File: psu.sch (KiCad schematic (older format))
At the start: 107 parts, among them J1 METER, J3 T1A, J4 T1B, J5 T1C, J6 SENSE+, J7 SENSE-, J8 OUT+, J9 OUT-, Q1 MMBT2907A, Q10 TIP105, Q11 MMBT2907A, Q12 MMBT2907A, Q13 PMP5201Y, Q14 MMBT3904, Q15 MMBT3904, Q16 MMBT3904, Q17 MMBT2907A, Q18 PZT2222A, Q2 MMBT2907A, Q3 MMBT3904, Q4 PMP4201Y, Q5 PMP5201Y, Q6 PMP4201Y, Q7 MMBT3904, Q8 MMBT2907A, Q9 MMBT2907A

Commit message: Changed local regulator circuit, added github readme
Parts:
- removed C4: 47u 10V, symbol C-ALUM-660
- removed Q1, Q2: MMBT2907A, symbol MMBT2907A
- removed R12: 2k2, symbol R-0805
- added Q1, Q2: MMBT3906, symbol MMBT3906
- C3: Manufacturer CDE -> (none); MouserPN 598-AVE106M35C12T-F -> (none); PartNo AVE106M35C12T-F -> (none)
- R11: value 22k -> 560
- R4, R5: value 10k -> 2k2
- R40: value 10k -> 100k
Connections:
- wire segments 279 -> 396
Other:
- note added: "ECO: Renumber\nECO: Check potentiometer rotation directions (library change?)"
- note added: "VOLTAGE REFERENCE and LOCAL REGULATOR"
- note removed: "ECO: Renumber\nECO: Add diodes to D2 for center-tapped (bodge is awkward)\nECO: Widen wire holes\nECO: Check potentiometer rotation directions (library change?)\nECO: Change C9 to same as C4\nECO: D3/DZ2 heat-sharing pad\nECO: Manual note about resistor source not mattering"
- note removed: "ERROR AMP\nBIAS"
- note removed: "LOCAL\nREGULATOR"
- note removed: "VOLTAGE REFERENCE"
- moved on the sheet: C5, D1, D2, D3, D4, D5, D6, D7, J3, J4, J5, Q4A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

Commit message: Rev C in progress
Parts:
- removed C1: 1000u 63V, symbol C-ALUM-16MM
- removed C10: 47u 63V, symbol C-ALUM-6.3MM
- removed C2: 47u, symbol C-ALUM-8MM
- removed C3: 10u, symbol C-ALUM-530
- removed C6: 33p 50V, symbol C-0805
- removed C7: 47u 10V, symbol C-ALUM-660
- removed C8: 10n, symbol C-0805
- removed D1: GBU 100V, symbol BRIDGE
- removed D10, D11, D12, D13: MMBD4148, symbol MMBD4148
- removed D2, D3: 1N4004, symbol 1N4004
- removed D4, D5, D6, D7: S1A, symbol S1A
- removed J6: SENSE+, symbol HEAD-F1
- removed J7: SENSE-, symbol HEAD-F1
- removed MP1, MP2, MP3, MP4: SCREW, symbol SCREW
- removed Q11, Q12: MMBT2907A, symbol MMBT2907A
- removed Q13, Q5: PMP5201Y, symbol PMP5201Y
- removed Q15: MMBT3904, symbol MMBT3904
- removed R15: 10k 1/2W, symbol R-1210
- removed R17: 150, symbol R-0805
- removed R18: 1k5, symbol R-0805
- removed R40: 100k, symbol R-0805
- removed RV1, RV4: 10k, symbol POT
- removed RV5, RV6: *, symbol POT
- added C1: 1000u 63V, symbol C-ALUM-16mm
- added C10: 1nF 1kV, symbol C-1206
- added C2, C6, C8: 47u 63V, symbol C-ALUM-6.3mm
- added C3: 100p, symbol C-0805
- added C5: 4u7, symbol C-1206
- added D1, D2, D3, D4, D5, D6, D7, D8: S1D, symbol S1D
- added J6: SENSE, symbol HEAD-F2
- added Q1, Q4: MMBT3906, symbol MMBT3906
- added Q10, Q19, Q20: MMBT2907A, symbol MMBT2907A
- added Q15: PZT2222A, symbol PZT2222A
- added Q16: MMBT3904, symbol MMBT3904
- added Q18, Q7: PMP4201Y, symbol PMP4201Y
- added R1, R27: 22k, symbol R-0805
- added R26: 100k, symbol R-0805
- added R28, R29: 1k, symbol R-0805
- added R30: 33, symbol R-0805
- added R31, R32: 10k, symbol R-0805
- added R45: 1Meg, symbol R-1206
- added RV2, RV4: 10k, symbol POT-TRIM
- added RV5, RV6: *, symbol POT-TRIM
- added TP1, TP2, TP3, TP4: GND, symbol TEST
- C4: renamed from C11; value 3n3 -> 1n; BomValueLine (none) -> CAP Ceramic 1nF 16V [0805]; OldReference (none) -> C4
- C7: renamed from C5; BomValueLine (none) -> CAP Ceramic 4.7uF 16V [1206]; OldReference (none) -> C7
- C9: BomValueLine (none) -> CAP Ceramic 4.7uF 16V [1206]; OldReference (none) -> C9
- D10: renamed from D9; OldReference (none) -> D10
- D11: renamed from D14; value S1A -> S1D; BomValueLine (none) -> DIODE 1A 50V [SMA]; OldReference (none) -> D11
- D12: renamed from D15; value S1A -> S1D; BomValueLine (none) -> DIODE 1A 50V [SMA]; OldReference (none) -> D12
- D9: renamed from D8; BomValueLine (none) -> DIODE Signal [SOT-23]; OldReference (none) -> D9
- DS1: value HOT -> LIM; BomValueLine (none) -> INDICATOR LED Red [Panel 6.35mm]; Manufacturer (none) -> Bivar; OldReference (none) -> DS1; PartNo (none) -> PM5RD
- DS2: value LIMIT -> HOT; BomValueLine (none) -> INDICATOR LED Red [Panel 6.35mm]; Manufacturer (none) -> Bivar; OldReference (none) -> DS2; PartNo (none) -> PM5RD
- DZ1: BomValueLine (none) -> DIODE Zener 6.2V 2% [SOT-23]; OldReference (none) -> DZ1
- DZ2: renamed from DZ3; BomValueLine (none) -> DIODE TVS 30V WPIV 33A IRSM [SMC-J]; OldReference (none) -> DZ2
- J1: OldReference (none) -> J1
- J3: OldReference (none) -> J3; PartNo (none) -> 60824-1
- J4: OldReference (none) -> J4; PartNo (none) -> 60824-1
- J5: OldReference (none) -> J5; PartNo (none) -> 60824-1
- J8: OldReference (none) -> J8; PartNo (none) -> 60824-1
- J9: OldReference (none) -> J9; PartNo (none) -> 60824-1
- Q11: renamed from Q6; BomValueLine (none) -> TRANS NPN Matched [SOT-363]; OldReference (none) -> Q11
- Q12: renamed from Q7; BomValueLine (none) -> TRANS NPN [SOT-23]; OldReference (none) -> Q12
- Q13: renamed from Q8; BomValueLine (none) -> TRANS PNP 60V [SOT-23]; OldReference (none) -> Q13
- Q14: BomValueLine (none) -> TRANS NPN [SOT-23]; OldReference (none) -> Q14
- Q17: renamed from Q10; BomValueLine (none) -> TRANS PNP Darlington hFE>=1000 60V w/Diode [TO-220]; OldReference (none) -> Q17
- Q2: renamed from Q3; BomValueLine (none) -> TRANS NPN [SOT-23]; OldReference (none) -> Q2
- Q21: renamed from Q17; BomValueLine (none) -> TRANS PNP [SOT-23]; OldReference (none) -> Q21
- Q22: renamed from Q16; BomValueLine (none) -> TRANS NPN [SOT-23]; OldReference (none) -> Q22
- Q3: renamed from Q18; BomValueLine (none) -> TRANS NPN [SOT-223]; OldReference (none) -> Q3
- Q5: renamed from Q2; BomValueLine (none) -> TRANS PNP [SOT-23]; OldReference (none) -> Q5
- Q6: renamed from Q1; BomValueLine (none) -> TRANS PNP [SOT-23]; OldReference (none) -> Q6
- Q8: renamed from Q4; BomValueLine (none) -> TRANS NPN Matched [SOT-363]; OldReference (none) -> Q8
- Q9: BomValueLine (none) -> TRANS PNP [SOT-23]; OldReference (none) -> Q9
- R10: renamed from R11; value 560 -> 470; BomValueLine (none) -> RES 470 5% [0805]; OldReference (none) -> R10
- R11: renamed from R6; value 12k -> 100k; BomValueLine (none) -> RES 100k 5% [0805]; OldReference (none) -> R11
- R12: renamed from R8; value 62k 1% -> 22k; BomValueLine (none) -> RES 22k 5% [0805]; OldReference (none) -> R12
- R13: renamed from R7; value 56k 1% -> 22k; BomValueLine (none) -> RES 22k 5% [0805]; OldReference (none) -> R13
- R14: renamed from R9; BomValueLine (none) -> RES 22k 0.5% [0805]; OldReference (none) -> R14
- R15: renamed from R10; BomValueLine (none) -> RES 22k 0.5% [0805]; OldReference (none) -> R15
- R16: BomValueLine (none) -> RES 1k 5% [0805]; OldReference (none) -> R16
- R17: renamed from R14; BomValueLine (none) -> RES 1k 5% [0805]; OldReference (none) -> R17
- R18: renamed from R13; OldReference (none) -> R18
- R19: value 820 -> 1k; BomValueLine (none) -> RES 1k 5% [0805]; OldReference (none) -> R19
- R2: value 4k7 -> 22k; BomValueLine (none) -> RES 22k 5% [0805]; OldReference (none) -> R2
- R20: value 12k -> 1k; BomValueLine (none) -> RES 1k 5% [0805]; OldReference (none) -> R20
- R21: value 1k -> 22k; BomValueLine (none) -> RES 22k 5% [0805]; OldReference (none) -> R21
- R22: BomValueLine (none) -> RES 1k 5% [0805]; OldReference (none) -> R22
- R23: value 10k -> 22k; BomValueLine (none) -> RES 22k 5% [0805]; OldReference (none) -> R23
- R24: value 8k2 -> 33; BomValueLine (none) -> RES 33 5% [0805]; OldReference (none) -> R24
- R25: BomValueLine (none) -> RES 10k 5% [0805]; OldReference (none) -> R25
- R3: renamed from R39; value 10 -> 33; BomValueLine (none) -> RES 33 5% [0805]; OldReference (none) -> R3
- R33: renamed from R34; BomValueLine (none) -> RES {1 / 0.47 / 1} 5% [1210]; OldReference (none) -> R33
- R34: renamed from R41; value 10k -> 22k; BomValueLine (none) -> RES 22k 5% [0805]; OldReference (none) -> R34
- R35: BomValueLine (none) -> RES {180 68 180} 5% [0805]; OldReference (none) -> R35
- R36: BomValueLine (none) -> RES {27k 15k 27k} 5% [0805]; OldReference (none) -> R36
- R37: renamed from R30; BomValueLine (none) -> RES 120k 0.5% [0805]; OldReference (none) -> R37
- R38: renamed from R31; BomValueLine (none) -> RES 120k 0.5% [0805]; OldReference (none) -> R38
- R39: renamed from R32; BomValueLine (none) -> RES 100 5% [0805]; OldReference (none) -> R39
- R4: value 2k2 -> 22k; BomValueLine (none) -> RES 22k 5% [0805]; OldReference (none) -> R4
- R40: renamed from R33; BomValueLine (none) -> RES 100 5% [0805]; OldReference (none) -> R40
- R41: renamed from R27; value 8k2 -> 10k; BomValueLine (none) -> RES 10k 5% [0805]; OldReference (none) -> R41
- R42: renamed from R26; BomValueLine (none) -> RES 100k 5% [0805]; OldReference (none) -> R42
- R43: renamed from R28; BomValueLine (none) -> RES Therm 100k 5% [Radial]; OldReference (none) -> R43
- R44: renamed from R29; BomValueLine (none) -> RES 270 5% [0805]; OldReference (none) -> R44
- R5: renamed from R37; value 27k -> 22k; BomValueLine (none) -> RES 22k 5% [0805]; OldReference (none) -> R5
- R6: renamed from R38; value 100k -> 18k; BomValueLine (none) -> RES 18k 5% [0805]; OldReference (none) -> R6
- R7: renamed from R3; value 22k -> 10k; BomValueLine (none) -> RES 10k 5% [0805]; OldReference (none) -> R7
- R8: renamed from R1; value 22k -> 10k; BomValueLine (none) -> RES 10k 5% [0805]; OldReference (none) -> R8
- R9: renamed from R5; value 2k2 -> 470; BomValueLine (none) -> RES 470 5% [0805]; OldReference (none) -> R9
- RV1: renamed from RV2; OldReference (none) -> RV1
- RV3: value 5k -> 10k; OldReference (none) -> RV3
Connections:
- net labels added: 1mA 240R, = MMBT2907A or similar (60V), = MMBT3904 or similar, = PMP4201Y, DMMT3904W or similar, = PMP5201Y, DMMT3906W or similar, CGND, GND, GUARD, V-UNREG
- net labels removed: 900uA 240R, = MMBT2907A, = MMBT3904, VBIAS, VCC, VEE
- wire segments 396 -> 291
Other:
- note added: "CURRENT LIMITER"
- note added: "ESR > 0r5"
- note added: "FEEDBACK INPUT"
- note added: "LOCAL REGULATOR"
- note added: "METER TRIM"
- note added: "Matching connector: TE Conn 60598-3\nConnectors are expensive and optional; holes will\ntake 16g wire as well."
- note added: "OUTPUT FILTER"
- note added: "POWER INPUT"
- note added: "R33"
- note added: "VOLTAGE REFERENCE"
- note removed: "CURRENT REFERENCE AND BIAS"
- note removed: "CURRENT SENSE RESISTOR"
- note removed: "CURRENT SENSE\nAMPLIFIER/\nCOMPARATOR"
- note removed: "ECO: Renumber\nECO: Check potentiometer rotation directions (library change?)"
- note removed: "MAIN\nRECTIFIER"
- note removed: "OUTPUT FILTER\nAND PROTECTION"
- note removed: "R34"
- note removed: "VOLTAGE REFERENCE and LOCAL REGULATOR"
- moved on the sheet: C4, C7, C9, D10, D11, D12, D9, DZ1, DZ2, J1, J3, J4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

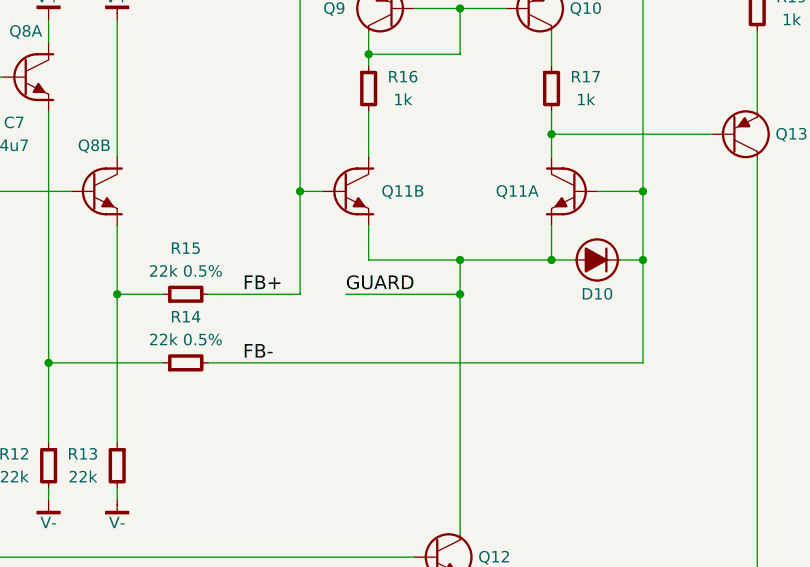
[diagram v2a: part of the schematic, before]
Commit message: Added beginning of simulation
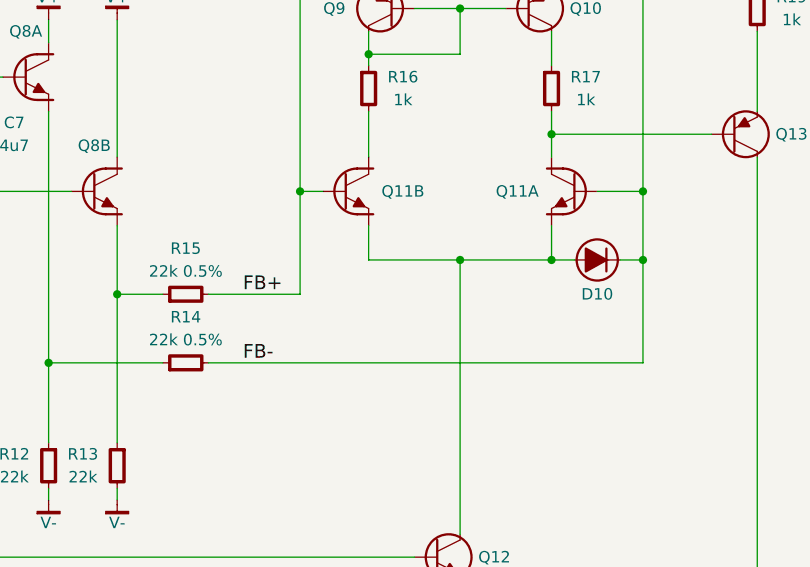
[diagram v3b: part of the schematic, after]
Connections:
- net labels removed: GUARD
- wire segments 291 -> 290
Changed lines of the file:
@@
 Connection ~ 5500 10000
-Wire Wire Line
-	7500 5150 7000 5150
-Connection ~ 7500 5150
-Text Label 7000 5150 0    60   ~ 0
-GUARD
 Wire Wire Line
 	10450 4600 10450 4700

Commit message: Few BOM-related changes
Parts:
- added DS3: POWER, symbol LED
- D10: BomValueLine (none) -> DIODE Signal [SOT-23]
- Q4: BomValueLine TRANS PNP 60V [SOT-23] -> TRANS PNP [SOT-23]
- R2: value 22k -> 10k; BomValueLine RES 22k 5% [0805] -> (none); OldReference R2 -> (none)
- R37, R38: value 120k 0.5% -> * 0.5%
- R39, R40: value 100 -> 270
- R45: BomValueLine (none) -> RES 1M 5% [1206]
- RV3: value 10k -> 1k
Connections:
- net labels added: 1A 125V SB
- net labels removed: 750mA 125V SB
- wire segments 290 -> 292
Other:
- note added: "120k"
- note added: "75k"
- note added: "Coupled\nto Q17"
- note added: "R37"
- note added: "R37, R38: 120k 75k 75k"
- note added: "R38"
- note removed: "Coupled\nto Q9"
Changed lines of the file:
@@
 F 2 "" H 8100 5000 60  0000 C CNN
 F 3 "" H 8100 5000 60  0000 C CNN
-F 4 "D10" H 8100 5000 50  0001 C CNN "OldReference"
+F 4 "DIODE Signal [SOT-23]" H 8100 5000 60  0001 C CNN "BomValueLine"
+F 5 "D10" H 8100 5000 50  0001 C CNN "OldReference"
 	1    8100 5000
 	0    -1   -1   0
@@
 P 12500 2200
 F 0 "R37" V 12300 2200 50  0000 C CNN
-F 1 "120k 0.5%" V 12400 2200 50  0000 C CNN
+F 1 "* 0.5%" V 12400 2200 50  0000 C CNN
 F 2 "" H 12500 2250 60  0000 C CNN
 F 3 "" H 12500 2250 60  0000 C CNN
@@
 P 13000 2300
 F 0 "R38" V 12700 2300 50  0000 C CNN
-F 1 "120k 0.5%" V 12800 2300 50  0000 C CNN
+F 1 "* 0.5%" V 12800 2300 50  0000 C CNN
 F 2 "" H 13000 2350 60  0000 C CNN
 F 3 "" H 13000 2350 60  0000 C CNN
@@
 P 13200 2800
 F 0 "R39" H 13350 2750 50  0000 C CNN
-F 1 "100" H 13350 2850 50  0000 C CNN
+F 1 "270" H 13350 2850 50  0000 C CNN
 F 2 "" H 13200 2850 60  0000 C CNN
 F 3 "" H 13200 2850 60  0000 C CNN
@@
 P 15000 7450
 F 0 "#FFP1" V 14900 7450 50  0001 C CNN
-F 1 "750mA 125V SB" V 14800 7450 50  0000 C CNN
+F 1 "1A 125V SB" V 14800 7450 50  0000 C CNN
 F 2 "" H 15000 7500 60  0000 C CNN
 F 3 "" H 15000 7500 60  0000 C CNN
@@
 $EndComp
 Text Notes 5650 2500 2    50   ~ 0
-Coupled\nto Q9
+Coupled\nto Q17
 $Comp
 L VA_METER #MFP1
@@
 P 15900 5150
 F 0 "#MFP1" H 16150 5100 50  0001 C CNN
-F 1 "1mA 240R" H 16250 5100 50  0000 C CNN
+F 1 "1mA 240R" H 16250 5200 50  0000 C CNN
 F 2 "" H 15900 5300 60  0000 C CNN
 F 3 "" H 15900 5300 60  0000 C CNN
 F 4 "METER 1mA full scale w/ custom scale card" H 15900 5150 60  0001 C CNN "BomValueLine"
-F 5 "M(FP)" H 16250 5200 50  0000 C CNN "Option"
+F 5 "M(FP)" H 16250 5100 50  0000 C CNN "Option"
 F 6 "#MFP1" H 15900 5150 50  0001 C CNN "OldReference"
 	1    15900 5150
@@
 	-1   0    0    -1
 $EndComp
-Text Notes 13850 3925 0    50   Italic 10
+Text Notes 13850 3675 0    50   Italic 10
 COMPONENT VALUES
-Text Notes 13850 4050 0    50   ~ 10
+Text Notes 13850 3800 0    50   ~ 10
 *
-Text Notes 14050 4050 0    50   ~ 10
+Text Notes 14050 3800 0    50   ~ 10
 PS-1H
-Text Notes 14400 4050 0    50   ~ 10
+Text Notes 14400 3800 0    50   ~ 10
 PS-1L
-Text Notes 14750 4050 0    50   ~ 10
+Text Notes 14750 3800 0    50   ~ 10
 PS-1LL
-Text Notes 13850 4250 0    50   ~ 10
+Text Notes 13850 4000 0    50   ~ 10
 R35
-Text Notes 14050 4250 0    50   ~ 0
+Text Notes 14050 4000 0    50   ~ 0
 180
-Text Notes 14400 4250 0    50   ~ 0
+Text Notes 14400 4000 0    50   ~ 0
 68
-Text Notes 14750 4250 0    50   ~ 0
+Text Notes 14750 4000 0    50   ~ 0
 180
-Text Notes 13850 4450 0    50   ~ 10
+Text Notes 13850 4200 0    50   ~ 10
 R36
-Text Notes 14050 4450 0    50   ~ 0
+Text Notes 14050 4200 0    50   ~ 0
 27k
-Text Notes 14400 4450 0    50   ~ 0
+Text Notes 14400 4200 0    50   ~ 0
 15k
-Text Notes 14750 4450 0    50   ~ 0
+Text Notes 14750 4200 0    50   ~ 0
 15k
-Text Notes 13850 4350 0    50   ~ 10
+Text Notes 13850 4100 0    50   ~ 10
 RV5
-Text Notes 14050 4350 0    50   ~ 0
+Text Notes 14050 4100 0    50   ~ 0
 500
-Text Notes 14400 4350 0    50   ~ 0
+Text Notes 14400 4100 0    50   ~ 0
 500
-Text Notes 14750 4350 0    50   ~ 0
+Text Notes 14750 4100 0    50   ~ 0
 500
-Text Notes 13850 4550 0    50   ~ 10
+Text Notes 13850 4300 0    50   ~ 10
 RV6
-Text Notes 14050 4550 0    50   ~ 0
+Text Notes 14050 4300 0    50   ~ 0
 20k
-Text Notes 14400 4550 0    50   ~ 0
+Text Notes 14400 4300 0    50   ~ 0
 10k
-Text Notes 14750 4550 0    50   ~ 0
+Text Notes 14750 4300 0    50   ~ 0
 10k
-Text Notes 13850 4150 0    50   ~ 10
+Text Notes 13850 3900 0    50   ~ 10
 R33
-Text Notes 14050 4150 0    50   ~ 0
+Text Notes 14050 3900 0    50   ~ 0
 1R
-Text Notes 14400 4150 0    50   ~ 0
+Text Notes 14400 3900 0    50   ~ 0
 R47
-Text Notes 14750 4150 0    50   ~ 0
+Text Notes 14750 3900 0    50   ~ 0
 1R
 $Comp
@@
 P 14150 2800
 F 0 "R40" H 14000 2750 50  0000 C CNN
-F 1 "100" H 14000 2850 50  0000 C CNN
+F 1 "270" H 14000 2850 50  0000 C CNN
 F 2 "" H 14150 2850 60  0000 C CNN
 F 3 "" H 14150 2850 60  0000 C CNN
@@
 P 10300 4750
 F 0 "RV3" H 10450 4800 50  0000 C CNN
-F 1 "10k" H 10450 4700 50  0000 C CNN
+F 1 "1k" H 10450 4700 50  0000 C CNN
 F 2 "" H 10300 4800 60  0000 C CNN
 F 3 "" H 10300 4800 60  0000 C CNN
@@
 F 2 "" H 5300 9650 60  0000 C CNN
 F 3 "" H 5300 9650 60  0000 C CNN
-F 4 "R45" H 5300 9600 50  0001 C CNN "OldReference"
+F 4 "RES 1M 5% [1206]" H 5300 9600 60  0001 C CNN "BomValueLine"
+F 5 "R45" H 5300 9600 50  0001 C CNN "OldReference"
 	1    5300 9600
 	0    -1   -1   0
@@
 Connection ~ 12300 7450
 Wire Notes Line
-	15100 3825 13825 3825
+	15100 3575 13825 3575
 Wire Notes Line
-	13825 3950 15100 3950
+	13825 3700 15100 3700
 Wire Notes Line
-	15100 4575 15100 3825
+	15100 3575 15100 4550
 Wire Notes Line
-	13825 4575 15100 4575
-Wire Notes Line
-	13825 3825 13825 4575
+	13825 3575 13825 4550
 Wire Wire Line
 	15000 5100 14850 5100
@@
 F 2 "" H 1750 4600 60  0000 C CNN
 F 3 "" H 1750 4600 60  0000 C CNN
-F 4 "TRANS PNP 60V [SOT-23]" H 1750 4600 60  0001 C CNN "BomValueLine"
+F 4 "TRANS PNP [SOT-23]" H 1750 4600 60  0001 C CNN "BomValueLine"
 F 5 "Q4" H 1750 4600 50  0001 C CNN "OldReference"
 	1    1750 4600
@@
 $EndComp
 Wire Wire Line
-	1000 5600 1000 6400
+	1000 5600 1000 6700
 $Comp
 L C-0805 C3
@@
 	1000 4900 1000 5400
 Connection ~ 1000 5300
-$Comp
-L R-0805 R2
-U 1 1 5326A50E
-P 1000 6500
-F 0 "R2" H 850 6550 50  0000 C CNN
-F 1 "22k" H 850 6450 50  0000 C CNN
-F 2 "" H 1000 6550 60  0000 C CNN
-F 3 "" H 1000 6550 60  0000 C CNN
-F 4 "RES 22k 5% [0805]" H 1000 6500 60  0001 C CNN "BomValueLine"
-F 5 "R2" H 1000 6500 50  0001 C CNN "OldReference"
-	1    1000 6500
-	1    0    0    -1
-$EndComp
-Wire Wire Line
-	1000 6600 1000 6700
 Wire Wire Line
 	1200 6800 1300 6800
@@
 	1    0    0    -1
 $EndComp
+Text Notes 11950 1900 0    50   ~ 0
+R37, R38: 120k 75k 75k
+Text Notes 13850 4400 0    50   ~ 10
+R37
+Text Notes 14050 4400 0    50   ~ 0
+120k
+Text Notes 14400 4400 0    50   ~ 0
+75k
+Text Notes 14750 4400 0    50   ~ 0
+75k
+Text Notes 13850 4500 0    50   ~ 10
+R38
+Text Notes 14050 4500 0    50   ~ 0
+120k
+Text Notes 14400 4500 0    50   ~ 0
+75k
+Text Notes 14750 4500 0    50   ~ 0
+75k
+Wire Notes Line
+	13825 4550 15100 4550
+$Comp
+L LED DS3
+U 1 1 532DFA05
+P 7500 9900
+F 0 "DS3" H 7850 9950 50  0000 C CNN
+F 1 "POWER" H 7850 9850 50  0000 C CNN
+F 2 "" H 7500 9900 60  0000 C CNN
+F 3 "" H 7500 9900 60  0000 C CNN
+F 4 "PM5RD" H 7500 9900 60  0001 C CNN "PartNo"
+F 5 "Bivar" H 7500 9900 60  0001 C CNN "Manufacturer"
+F 6 "INDICATOR LED Red [Panel 6.35mm]" H 7500 9900 60  0001 C CNN "BomValueLine"
+F 7 "DS1" H 7500 9900 50  0001 C CNN "OldReference"
+	1    7500 9900
+	1    0    0    -1
+$EndComp
+Wire Wire Line
+	7500 10050 7500 10000
+$Comp
+L R-0805 R2
+U 1 1 532DFBBF
+P 7500 9600
+F 0 "R2" H 7750 9650 50  0000 C CNN
+F 1 "10k" H 7750 9550 50  0000 C CNN
+F 2 "" H 7500 9650 60  0000 C CNN
+F 3 "" H 7500 9650 60  0000 C CNN
+	1    7500 9600
+	1    0    0    -1
+$EndComp
+$Comp
+L V-UNREG #PWR041
+U 1 1 532DFBD3
+P 7500 10050
+F 0 "#PWR041" H 7500 10000 30  0001 C CNN
+F 1 "V-UNREG" H 7500 9950 50  0000 C CNN
+F 2 "" H 7500 10050 60  0000 C CNN
+F 3 "" H 7500 10050 60  0000 C CNN
+	1    7500 10050
+	1    0    0    -1
+$EndComp
+$Comp
+L V+ #PWR042
+U 1 1 532DFBE7
+P 7500 9450
+F 0 "#PWR042" H 7500 9500 30  0001 C CNN
+F 1 "V+" H 7500 9550 50  0000 C CNN
+F 2 "" H 7500 9450 60  0000 C CNN
+F 3 "" H 7500 9450 60  0000 C CNN
+	1    7500 9450
+	1    0    0    -1
+$EndComp
+Wire Wire Line
+	7500 9450 7500 9500
+Wire Wire Line
+	7500 9700 7500 9800
 $EndSCHEMATC
